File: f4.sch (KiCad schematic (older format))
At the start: 4 parts, among them SW1 SW_Push

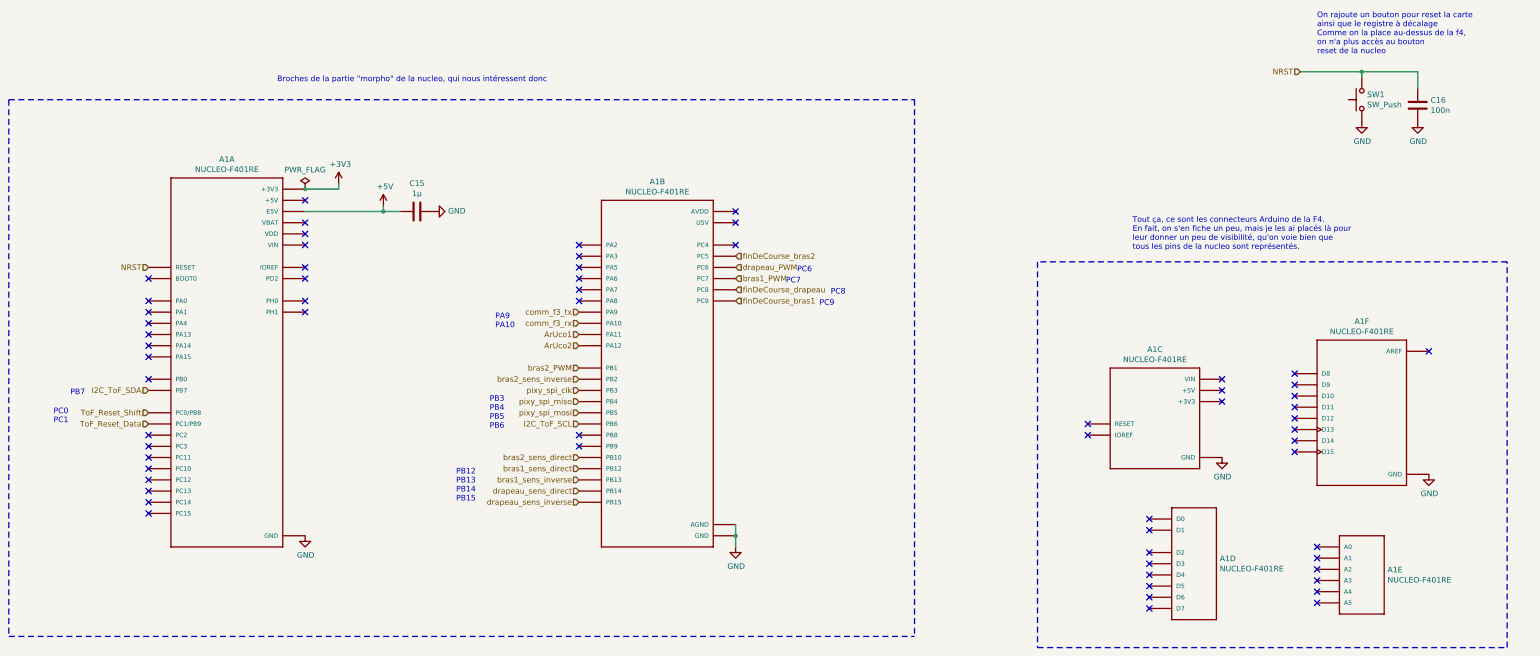
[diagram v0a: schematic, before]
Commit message: removed psi-things pins, added transceiver MCP2551 for CAN, changed motors input protocol, RS must be chosen 1 or 10 kohms, and a foot print for a potentitial 120 ohms resistor is present for CAN bus end.
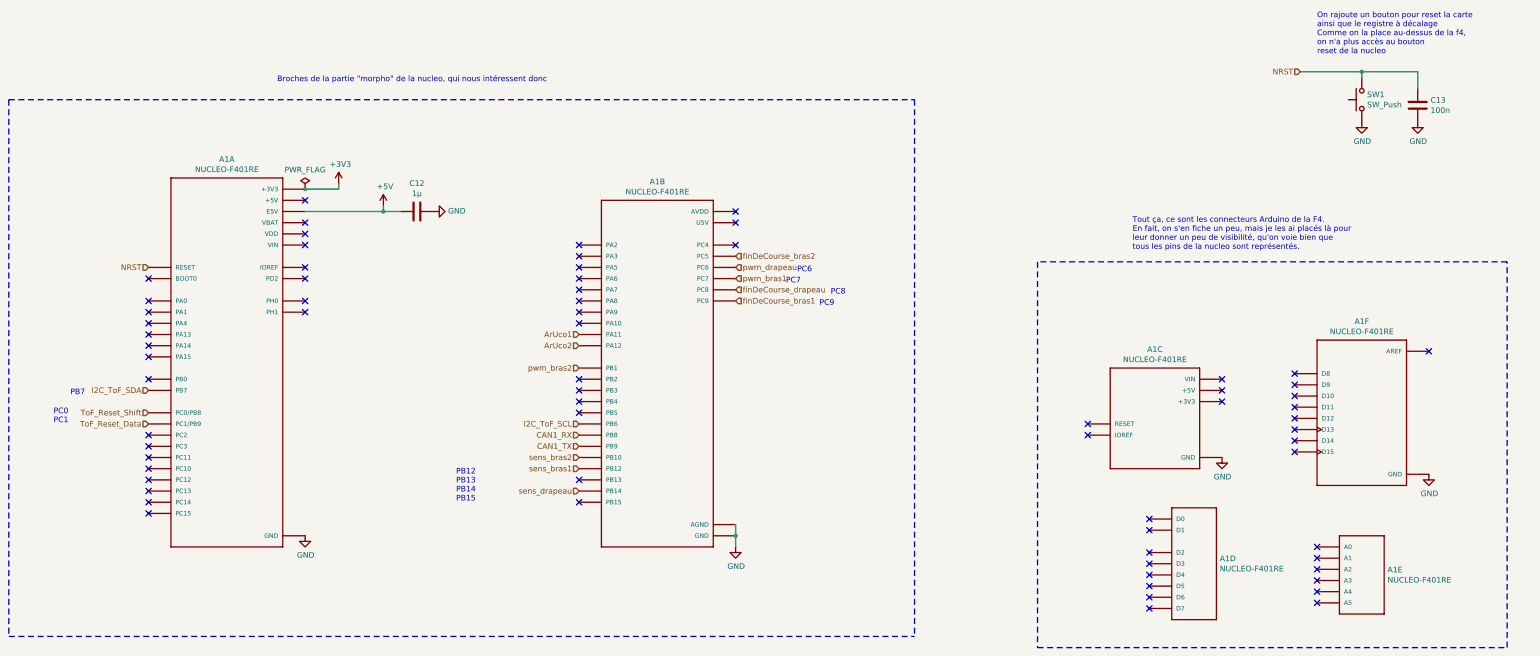
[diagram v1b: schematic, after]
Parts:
- renumbered C15 to C12, C16 to C13
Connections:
- net CAN1_RX: now reaches A1.CN10_3 (PB8)
- net CAN1_TX: now reaches A1.CN10_5 (PB9)
- net bras1_PWM renamed pwm_bras1
- net bras1_sens_direct renamed sens_bras1
- net bras1_sens_inverse: no longer names the net of A1.CN10_30 (PB13)
- net bras2_PWM renamed pwm_bras2
- net bras2_sens_direct renamed sens_bras2
- net bras2_sens_inverse: no longer names the net of A1.CN10_22 (PB2)
- net comm_f3_rx: no longer names the net of A1.CN10_33 (PA10)
- net comm_f3_tx: no longer names the net of A1.CN10_21 (PA9)
- net drapeau_PWM renamed pwm_drapeau
- net drapeau_sens_direct renamed sens_drapeau
- net drapeau_sens_inverse: no longer names the net of A1.CN10_26 (PB15)
- net pixy_spi_clk: no longer names the net of A1.CN10_31 (PB3)
- net pixy_spi_miso: no longer names the net of A1.CN10_27 (PB4)
- net pixy_spi_mosi: no longer names the net of A1.CN10_29 (PB5)
- no-connect marks 63 -> 69
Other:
- note removed: "PA9\nPA10\n"
- note removed: "PB3\nPB4\nPB5\nPB6\n"
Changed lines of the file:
@@
 $Descr A3 16535 11693
 encoding utf-8
-Sheet 21 24
+Sheet 19 23
 Title ""
 Date ""
@@
 ToF_Reset_Data
 Text HLabel 6800 5700 0    50   Input ~ 0
-drapeau_sens_direct
+sens_drapeau
 Text HLabel 6800 5500 0    50   Input ~ 0
-bras1_sens_direct
-Text HLabel 6800 5800 0    50   Input ~ 0
-drapeau_sens_inverse
-Text HLabel 6800 5600 0    50   Input ~ 0
-bras1_sens_inverse
-Text HLabel 6800 4100 0    50   Input ~ 0
-comm_f3_tx
-Text HLabel 6800 4200 0    50   Input ~ 0
-comm_f3_rx
+sens_bras1
 Text HLabel 13250 1950 0    50   Input ~ 0
 NRST
@@
 P 14300 2250
 AR Path="/5E811168/5E81E95C" Ref="C?"  Part="1"
-AR Path="/5E6933BA/5E81E95C" Ref="C16"  Part="1"
-F 0 "C16" H 14415 2296 50  0000 L CNN
+AR Path="/5E6933BA/5E81E95C" Ref="C13"  Part="1"
+F 0 "C13" H 14415 2296 50  0000 L CNN
 F 1 "100n" H 14415 2205 50  0000 L CNN
 F 2 "Capacitor_SMD:C_0805_2012Metric_Pad1.15x1.40mm_HandSolder" H 14338 2100 50  0001 C CNN
@@
 P 14300 2400
 AR Path="/5E811168/5E81E962" Ref="#PWR?"  Part="1"
-AR Path="/5E6933BA/5E81E962" Ref="#PWR067"  Part="1"
-F 0 "#PWR067" H 14300 2150 50  0001 C CNN
+AR Path="/5E6933BA/5E81E962" Ref="#PWR056"  Part="1"
+F 0 "#PWR056" H 14300 2150 50  0001 C CNN
 F 1 "GND" H 14305 2227 50  0000 C CNN
 F 2 "" H 14300 2400 50  0001 C CNN
@@
 P 13800 2400
 AR Path="/5E811168/5E81E968" Ref="#PWR?"  Part="1"
-AR Path="/5E6933BA/5E81E968" Ref="#PWR066"  Part="1"
-F 0 "#PWR066" H 13800 2150 50  0001 C CNN
+AR Path="/5E6933BA/5E81E968" Ref="#PWR055"  Part="1"
+F 0 "#PWR055" H 13800 2150 50  0001 C CNN
 F 1 "GND" H 13805 2227 50  0000 C CNN
 F 2 "" H 13800 2400 50  0001 C CNN
@@
 Text Notes 2100 5100 0    50   ~ 0
 PC0\nPC1\n
-Text Notes 6050 4250 0    50   ~ 0
-PA9\nPA10\n
 Text Notes 5700 5800 0    50   ~ 0
 PB12\nPB13\nPB14\nPB15
@@
 	1    0    0    -1
 $EndComp
-Text Notes 6000 5150 0    50   ~ 0
-PB3\nPB4\nPB5\nPB6\n
-Text HLabel 6800 5000 0    50   Input ~ 0
-pixy_spi_mosi
-Text HLabel 6800 4900 0    50   Input ~ 0
-pixy_spi_miso
-Text HLabel 6800 4800 0    50   Input ~ 0
-pixy_spi_clk
 Text HLabel 6800 5100 0    50   Input ~ 0
 I2C_ToF_SCL
@@
 PC6\n
 Text HLabel 8200 3700 2    50   Input ~ 0
-drapeau_PWM
+pwm_drapeau
 Text Notes 8650 3850 0    50   ~ 0
 PC7\n
 Text HLabel 8200 3800 2    50   Input ~ 0
-bras1_PWM
+pwm_bras1
 Text Notes 2250 4850 0    50   ~ 0
 PB7\n
 $Comp
-L shield_etage2-rescue:+5V-power-shield_etage2-rescue #PWR062
+L shield_etage2-rescue:+5V-power-shield_etage2-rescue #PWR051
 U 1 1 5E8EEA6E
 P 5050 3150
-F 0 "#PWR062" H 5050 3000 50  0001 C CNN
+F 0 "#PWR051" H 5050 3000 50  0001 C CNN
 F 1 "+5V" H 5065 3323 50  0000 C CNN
 F 2 "" H 5050 3150 50  0001 C CNN
@@
 $EndComp
 $Comp
-L shield_etage2-rescue:C-Device-shield_etage2-rescue C15
+L shield_etage2-rescue:C-Device-shield_etage2-rescue C12
 U 1 1 5E8F04FC
 P 5350 3200
-F 0 "C15" V 5602 3200 50  0000 C CNN
+F 0 "C12" V 5602 3200 50  0000 C CNN
 F 1 "1µ" V 5511 3200 50  0000 C CNN
 F 2 "Capacitor_SMD:C_0805_2012Metric_Pad1.15x1.40mm_HandSolder" H 5388 3050 50  0001 C CNN
@@
 $EndComp
 $Comp
-L shield_etage2-rescue:GND-power-shield_etage2-rescue #PWR063
+L shield_etage2-rescue:GND-power-shield_etage2-rescue #PWR052
 U 1 1 5E8F1C24
 P 5500 3200
-F 0 "#PWR063" H 5500 2950 50  0001 C CNN
+F 0 "#PWR052" H 5500 2950 50  0001 C CNN
 F 1 "GND" V 5505 3072 50  0000 R CNN
 F 2 "" H 5500 3200 50  0001 C CNN
@@
 Connection ~ 5050 3200
 $Comp
-L shield_etage2-rescue:GND-power-shield_etage2-rescue #PWR060
+L shield_etage2-rescue:GND-power-shield_etage2-rescue #PWR049
 U 1 1 5E8F67E4
 P 4350 6100
-F 0 "#PWR060" H 4350 5850 50  0001 C CNN
+F 0 "#PWR049" H 4350 5850 50  0001 C CNN
 F 1 "GND" H 4355 5927 50  0000 C CNN
 F 2 "" H 4350 6100 50  0001 C CNN
@@
 $EndComp
 $Comp
-L shield_etage2-rescue:GND-power-shield_etage2-rescue #PWR064
+L shield_etage2-rescue:GND-power-shield_etage2-rescue #PWR053
 U 1 1 5E8F7826
 P 8200 6200
-F 0 "#PWR064" H 8200 5950 50  0001 C CNN
+F 0 "#PWR053" H 8200 5950 50  0001 C CNN
 F 1 "GND" H 8205 6027 50  0000 C CNN
 F 2 "" H 8200 6200 50  0001 C CNN
@@
 $EndComp
 $Comp
-L shield_etage2-rescue:GND-power-shield_etage2-rescue #PWR068
+L shield_etage2-rescue:GND-power-shield_etage2-rescue #PWR057
 U 1 1 5E8FE2BA
 P 14400 5550
-F 0 "#PWR068" H 14400 5300 50  0001 C CNN
+F 0 "#PWR057" H 14400 5300 50  0001 C CNN
 F 1 "GND" H 14405 5377 50  0000 C CNN
 F 2 "" H 14400 5550 50  0001 C CNN
@@
 $EndComp
 $Comp
-L shield_etage2-rescue:GND-power-shield_etage2-rescue #PWR065
+L shield_etage2-rescue:GND-power-shield_etage2-rescue #PWR054
 U 1 1 5E8FEF08
 P 12550 5400
-F 0 "#PWR065" H 12550 5150 50  0001 C CNN
+F 0 "#PWR054" H 12550 5150 50  0001 C CNN
 F 1 "GND" H 12555 5227 50  0000 C CNN
 F 2 "" H 12550 5400 50  0001 C CNN
@@
 NoConn ~ 2950 5800
 NoConn ~ 2950 5900
-NoConn ~ 6800 5300
-NoConn ~ 6800 5200
 NoConn ~ 11350 5100
 NoConn ~ 11350 5200
@@
 NoConn ~ 11900 5950
 $Comp
-L shield_etage2-rescue:+3V3-power-shield_etage2-rescue #PWR061
+L shield_etage2-rescue:+3V3-power-shield_etage2-rescue #PWR050
 U 1 1 5E93C2F8
 P 4650 2950
-F 0 "#PWR061" H 4650 2800 50  0001 C CNN
+F 0 "#PWR050" H 4650 2800 50  0001 C CNN
 F 1 "+3V3" H 4665 3123 50  0000 C CNN
 F 2 "" H 4650 2950 50  0001 C CNN
@@
 	4650 3000 4650 2950
 $Comp
-L shield_etage2-rescue:PWR_FLAG-power-shield_etage2-rescue #FLG05
+L shield_etage2-rescue:PWR_FLAG-power-shield_etage2-rescue #FLG04
 U 1 1 5E94097F
 P 4350 3000
-F 0 "#FLG05" H 4350 3075 50  0001 C CNN
+F 0 "#FLG04" H 4350 3075 50  0001 C CNN
 F 1 "PWR_FLAG" H 4350 3173 50  0000 C CNN
 F 2 "" H 4350 3000 50  0001 C CNN
@@
 ArUco2
 Text HLabel 6800 4600 0    50   Input ~ 0
-bras2_PWM
-Text HLabel 6800 4700 0    50   Input ~ 0
-bras2_sens_inverse
+pwm_bras2
 Text HLabel 6800 5400 0    50   Input ~ 0
-bras2_sens_direct
+sens_bras2
 Text HLabel 8200 3600 2    50   Input ~ 0
 finDeCourse_bras2
+NoConn ~ 6800 4100
+NoConn ~ 6800 4200
+Text HLabel 6800 5300 0    50   Input ~ 0
+CAN1_TX
+Text HLabel 6800 5200 0    50   Input ~ 0
+CAN1_RX
+NoConn ~ 6800 4800
+NoConn ~ 6800 4900
+NoConn ~ 6800 5000
+NoConn ~ 6800 4700
+NoConn ~ 6800 5600
+NoConn ~ 6800 5800
 $EndSCHEMATC

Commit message: correction mm -> inch, empreinte du bouton
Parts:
- SW1: footprint Button_Switch_SMD:SW_Push_1P1T_NO_6x6mm_H9.5mm -> button:5x5
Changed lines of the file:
@@
 F 0 "SW1" V 13846 2152 50  0000 R CNN
 F 1 "SW_Push" V 13755 2152 50  0000 R CNN
-F 2 "Button_Switch_SMD:SW_Push_1P1T_NO_6x6mm_H9.5mm" H 13800 2400 50  0001 C CNN
+F 2 "button:5x5" H 13800 2400 50  0001 C CNN
 F 3 "~" H 13800 2400 50  0001 C CNN
 	1    13800 2200
